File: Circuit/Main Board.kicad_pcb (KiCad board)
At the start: 2 copper layers, 120 x 120 mm, 200 parts, among them J1 Conn_Coaxial, J2 Conn_Coaxial, J3 Conn_Coaxial, J4 Conn_Coaxial, J5 Conn_01x02_Pin, J6 Conn_01x03_Pin, J7 Conn_01x02_Pin, J8 Conn_01x02_Pin, J9 Conn_01x05_Pin, K1 AGQ200A12, K2 AGQ200A12, K3 AGQ200A12, K4 AGQ200A12, K5 AGQ200A12, K6 AGQ200A12, K7 AGQ200A12, Q1 2N7002, Q2 TIP41C, Q3 TIP42C, Q4 TIP41C, Q5 TIP42C, Q6 TIP41C, Q7 TIP42C, U1 STM32G491CCUx, U10 OPA2197xD, U11 INA828D, U12 DG201, U13 OPA2197xD, U14 DG201, U15 OPA2376xxD, U16 INA828D, U17 DG201, U18 OPA2376xxD, U2 DG201, U3 OPA2197xD, U4 OPA2197xD, U5 OPA2197xD, U6 OPA2197xD, U7 ULN2003, U8 DG201, U9 OPA2376xxD, Y1 ECS-2520MV-xxx-xx

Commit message: Update Main Board.kicad_pcb
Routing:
- net /Auto-Balancing Bridge/In: track 141.8 -> 138.6 mm

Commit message: Update Main Board.kicad_pcb
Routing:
- net GND: vias 124 -> 130
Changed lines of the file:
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@@
 	)
 	(via
+		(at 158.877 89.027)
+		(size 0.6)
+		(drill 0.3)
+		(layers "F.Cu" "B.Cu")
+		(free yes)
+		(net 50)
+	)
+	(via
+		(at 150.368 151.13)
+		(size 0.6)
+		(drill 0.3)
+		(layers "F.Cu" "B.Cu")
+		(free yes)
+		(net 50)
+	)
+	(via
 		(at 88.392 140.97)
 		(size 0.6)
@@
 	)
 	(via
+		(at 158.877 125.73)
+		(size 0.6)
+		(drill 0.3)
+		(layers "F.Cu" "B.Cu")
+		(free yes)
+		(net 50)
+	)
+	(via
 		(at 88.265 44.45)
 		(size 0.6)
@@
 	)
 	(via
+		(at 147.32 154.94)
+		(size 0.6)
+		(drill 0.3)
+		(layers "F.Cu" "B.Cu")
+		(free yes)
+		(net 50)
+	)
+	(via
 		(at 115.57 86.36)
 		(size 0.6)
@@
 	)
 	(via
+		(at 153.162 144.78)
+		(size 0.6)
+		(drill 0.3)
+		(layers "F.Cu" "B.Cu")
+		(free yes)
+		(net 50)
+	)
+	(via
 		(at 113.157 64.262)
 		(size 0.6)
@@
 	)
 	(via
+		(at 153.67 154.94)
+		(size 0.6)
+		(drill 0.3)
+		(layers "F.Cu" "B.Cu")
+		(free yes)
+		(net 50)
+	)
+	(via
 		(at 99.695 62.865)
 		(size 0.6)
@@
 	)
 	(segment
-		(start 149.479 149.479)
-		(end 149.479 153.659886)
+		(start 144.78 147.701)
+		(end 147.955 147.701)
 		(width 0.5)
 		(layer "F.Cu")
@@
 	)
 	(segment
-		(start 140.8195 143.7405)
-		(end 144.399 147.32)
+		(start 148.717 157.226)
+		(end 149.479 156.464)
 		(width 0.5)
 		(layer "F.Cu")
@@
 	)
 	(segment
-		(start 148.717 157.226)
-		(end 149.479 156.464)
+		(start 149.479 156.464)
+		(end 149.479 153.659886)
 		(width 0.5)
 		(layer "F.Cu")
@@
 	)
 	(segment
-		(start 149.479 156.464)
-		(end 149.479 153.659886)
+		(start 140.8195 130.175)
+		(end 140.8195 143.7405)
 		(width 0.5)
 		(layer "F.Cu")
@@
 	)
 	(segment
-		(start 144.399 147.32)
-		(end 147.32 147.32)
+		(start 149.479 149.225)
+		(end 149.479 153.659886)
 		(width 0.5)
 		(layer "F.Cu")
@@
 	)
 	(segment
-		(start 140.8195 130.175)
-		(end 140.8195 143.7405)
+		(start 140.8195 143.7405)
+		(end 144.78 147.701)
 		(width 0.5)
 		(layer "F.Cu")
@@
 	)
 	(segment
-		(start 147.32 147.32)
-		(end 149.479 149.479)
+		(start 147.955 147.701)
+		(end 149.479 149.225)
 		(width 0.5)
 		(layer "F.Cu")
@@
 		(min_thickness 0.25)
 		(filled_areas_thickness no)
-		(fill
+		(fill yes
 			(thermal_gap 0.5)
 			(thermal_bridge_width 0.5)
@@
 		(min_thickness 0.25)
 		(filled_areas_thickness no)
-		(fill
+		(fill yes
 			(thermal_gap 0.5)
 			(thermal_bridge_width 0.5)

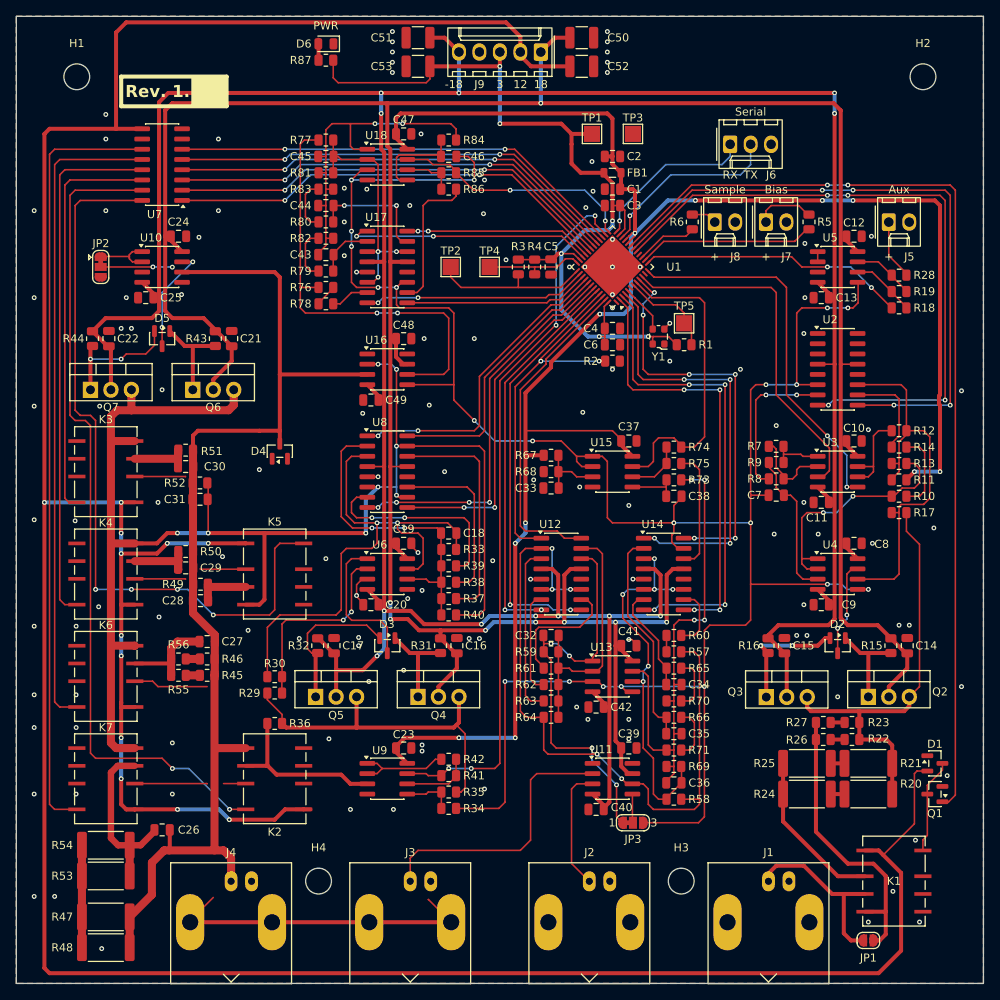
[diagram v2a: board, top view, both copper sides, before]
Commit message: Input Protection Second Attempt
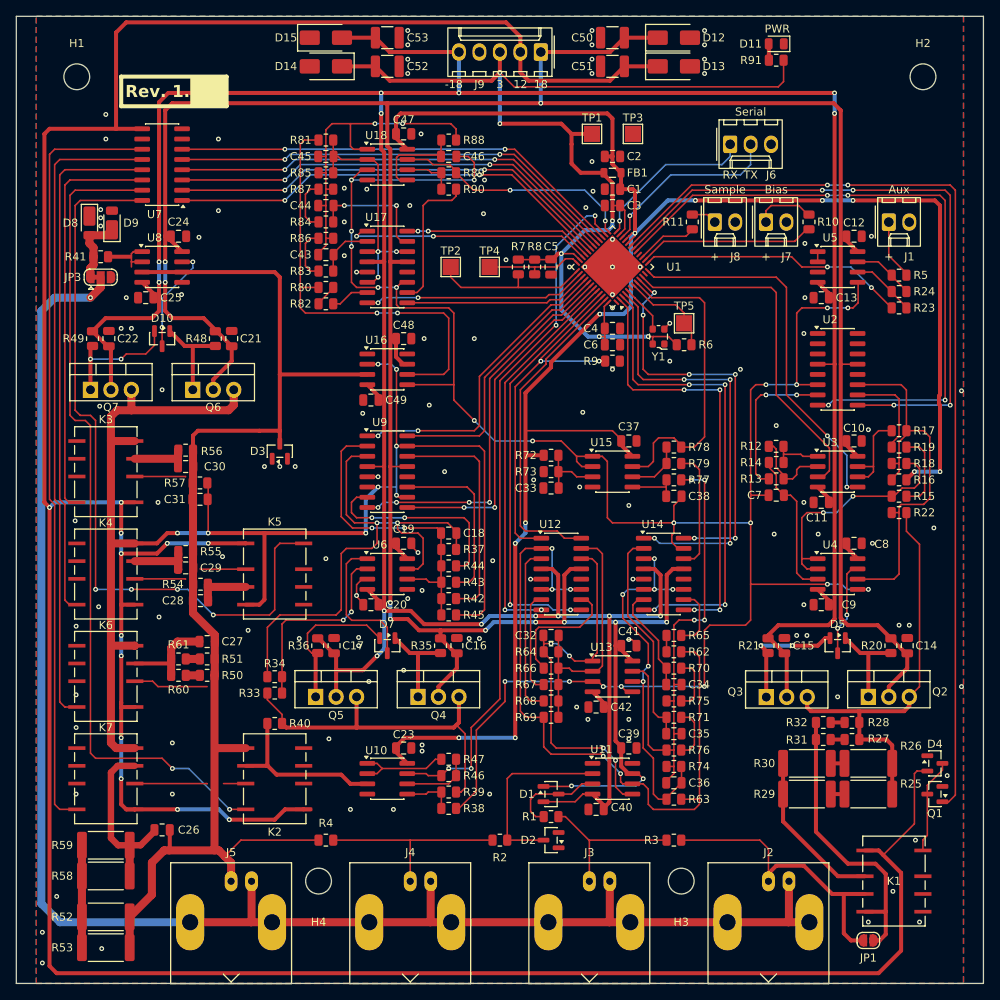
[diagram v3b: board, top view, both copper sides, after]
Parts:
- removed the C51 at (91.4, 45.2)
- removed the D4 at (74.3, 96.5)
- removed JP2: SolderJumper_3_Bridged12, Jumper:SolderJumper-3_P1.3mm_Bridged12_RoundedPad1.0x1.5mm
- removed the R28 at (151.1, 74.7)
- added C53: 22u, Capacitor_SMD:C_1210_3225Metric, F.Cu at (87.6, 45.2)
- added D1: BAV199, Package_TO_SOT_SMD:SOT-23, F.Cu at (108.0, 139.1)
- added D12: TBD, Diode_SMD:D_SMA, F.Cu at (123.2, 45.2)
- added D13: TBD, Diode_SMD:D_SMA, F.Cu at (123.2, 48.8)
- added D14: TBD, Diode_SMD:D_SMA, F.Cu at (80.0, 48.8)
- added D15: TBD, Diode_SMD:D_SMA, F.Cu at (80.0, 45.2)
- added D2: BAV199, Package_TO_SOT_SMD:SOT-23, F.Cu at (108.0, 144.8)
- added D3: BAV199, Package_TO_SOT_SMD:SOT-23, F.Cu at (74.3, 96.5)
- added D8: DFLS240LX, Diode_SMD:D_PowerDI-123, F.Cu at (50.7, 68.2)
- added D9: DFLS240LX, Diode_SMD:D_PowerDI-123, F.Cu at (53.5, 68.2)
- added R1: 1k, Resistor_SMD:R_0805_2012Metric, F.Cu at (108.0, 141.9)
- added R2: 1k, Resistor_SMD:R_0805_2012Metric, F.Cu at (101.6, 144.8)
- added R3: 100k, Resistor_SMD:R_0805_2012Metric, F.Cu at (123.2, 144.8)
- added R4: 100k, Resistor_SMD:R_0805_2012Metric, F.Cu at (80.0, 144.8)
- added R41: 50, Resistor_SMD:R_0805_2012Metric, F.Cu at (52.1, 72.4)
- added R5: 50, Resistor_SMD:R_0805_2012Metric, F.Cu at (151.1, 74.7)
- JP3: footprint Jumper:SolderJumper-3_P1.3mm_Bridged12_RoundedPad1.0x1.5mm_NumberLabels -> Jumper:SolderJumper-3_P1.3mm_Bridged12_RoundedPad1.0x1.5mm
- moved JP3 94.6 mm to (52.1, 74.9)
- moved D11 55.9 mm to (135.9, 46.0)
- moved R91 55.9 mm to (135.9, 48.0)
- moved C52 3.81 mm to (87.6, 48.8), turned to 180 degrees
- moved C50 3.81 mm to (115.6, 45.2), turned to 0 degrees
- moved C51 3.81 mm to (115.6, 48.8), turned to 0 degrees
- renumbered C52 to C51, C53 to C52, D5 to D10, D6 to D11, D1 to D4, D2 to D5, D3 to D7, J5 to J1, J1 to J2, J2 to J3, J3 to J4, J4 to J5, R5 to R10, R6 to R11, R7 to R12, R8 to R13, R9 to R14, R10 to R15, R11 to R16, R12 to R17, R13 to R18, R14 to R19, R15 to R20, R16 to R21, R17 to R22, R18 to R23, R19 to R24, R20 to R25, R21 to R26, R22 to R27, R23 to R28, R24 to R29, R25 to R30, R26 to R31, R27 to R32, R29 to R33, R30 to R34, R31 to R35, R32 to R36, R33 to R37, R34 to R38, R35 to R39, R36 to R40, R37 to R42, R38 to R43, R39 to R44, R40 to R45, R41 to R46, R42 to R47, R43 to R48, R44 to R49, R45 to R50, R46 to R51, R47 to R52, R48 to R53, R49 to R54, R50 to R55, R51 to R56, R52 to R57, R53 to R58, R54 to R59, R1 to R6, R55 to R60, R56 to R61, R57 to R62, R58 to R63, R59 to R64, R60 to R65, R61 to R66, R62 to R67, R63 to R68, R64 to R69, R3 to R7, R65 to R70, R66 to R71, R67 to R72, R68 to R73, R69 to R74, R70 to R75, R71 to R76, R73 to R77, R74 to R78, R75 to R79, R4 to R8, R76 to R80, R77 to R81, R78 to R82, R79 to R83, R80 to R84, R81 to R85, R82 to R86, R83 to R87, R84 to R88, R85 to R89, R2 to R9, R86 to R90, R87 to R91, U9 to U10, U10 to U8, U8 to U9
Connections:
- C26 pad 1: /Auto-Balancing Bridge/In -> /Auto-Balancing Bridge/TIA_SUM
- C27 pad 1: /Auto-Balancing Bridge/In -> /Auto-Balancing Bridge/TIA_SUM
- C28 pad 1: /Auto-Balancing Bridge/In -> /Auto-Balancing Bridge/TIA_SUM
- C29 pad 1: /Auto-Balancing Bridge/In -> /Auto-Balancing Bridge/TIA_SUM
- C30 pad 1: /Auto-Balancing Bridge/In -> /Auto-Balancing Bridge/TIA_SUM
- C31 pad 1: /Auto-Balancing Bridge/In -> /Auto-Balancing Bridge/TIA_SUM
- C32 pad 1: Net-(JP3-A) -> Net-(U11-Ref)
- J1 pad 1: /Signal Source/Aux_Out -> Net-(J1-Pin_1)
- J2 pad 2: GND -> GUARD EXT
- J3 pad 1: /Voltage Amplifier/In+ -> Net-(J3-In)
- J3 pad 2: GND -> GUARD EXT
- J4 pad 1: /Voltage Amplifier/In- -> Net-(J4-In)
- J4 pad 2: GUARD -> GUARD EXT
- J5 pad 1: /Auto-Balancing Bridge/In -> /Auto-Balancing Bridge/TIA_SUM
- J5 pad 2: GUARD -> GUARD EXT
- JP3 pad 1: Net-(JP3-A) -> Net-(D8-A)
- JP3 pad 2: Net-(JP3-C) -> GUARD EXT
- JP3 pad 3: +1.65VA -> GND
- K2 pad 5: /Auto-Balancing Bridge/In -> /Auto-Balancing Bridge/TIA_SUM
- K3 pad 2: GUARD -> unconnected-(K3-Pad2)
- K4 pad 2: GUARD -> unconnected-(K4-Pad2)
- K5 pad 2: GUARD -> unconnected-(K5-Pad2)
- K6 pad 2: GUARD -> unconnected-(K6-Pad2)
- K7 pad 2: GUARD -> unconnected-(K7-Pad2)
- R24 pad 2: Net-(R19-Pad2) (its old number) -> /Signal Source/Aux_Out
- R50 pad 1: /Auto-Balancing Bridge/In -> /Auto-Balancing Bridge/TIA_SUM
- R51 pad 1: /Auto-Balancing Bridge/In -> /Auto-Balancing Bridge/TIA_SUM
- R52 pad 1: /Auto-Balancing Bridge/In -> /Auto-Balancing Bridge/TIA_SUM
- R53 pad 1: /Auto-Balancing Bridge/In -> /Auto-Balancing Bridge/TIA_SUM
- R54 pad 1: /Auto-Balancing Bridge/In -> /Auto-Balancing Bridge/TIA_SUM
- R55 pad 1: /Auto-Balancing Bridge/In -> /Auto-Balancing Bridge/TIA_SUM
- R56 pad 1: /Auto-Balancing Bridge/In -> /Auto-Balancing Bridge/TIA_SUM
- R57 pad 1: /Auto-Balancing Bridge/In -> /Auto-Balancing Bridge/TIA_SUM
- R64 pad 1: Net-(JP3-A) -> Net-(U11-Ref)
- U11 pad 5: Net-(JP3-C) -> Net-(U11-Ref)
- U12 pad 14: Net-(JP3-A) -> Net-(U11-Ref)
- U13 pad 1: Net-(JP3-A) -> Net-(U11-Ref)
- U16 pad 3: /Auto-Balancing Bridge/In -> /Auto-Balancing Bridge/TIA_SUM
- U5 pad 7: Net-(R19-Pad2) (its old number) -> /Signal Source/Aux_Out
- U8 pad 1: Net-(JP2-A) -> GUARD
- U8 pad 2: Net-(JP2-A) -> GUARD
- U8 pad 3: GND -> /Auto-Balancing Bridge/TIA_SUM
- U8 pad 6: /Auto-Balancing Bridge/In -> /Auto-Balancing Bridge/TIA_SUM
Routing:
- net GUARD EXT: track 0.00 -> 200.7 mm, vias 0 -> 1
- net /Auto-Balancing Bridge/TIA_SUM: track 0.00 -> 155.7 mm
- net /Auto-Balancing Bridge/In: track 138.6 -> 0.00 mm
- net Net-(JP3-A): track 51.3 -> 0.00 mm, vias 4 -> 0
- net Net-(U11-Ref): track 0.00 -> 49.8 mm, vias 0 -> 4
- net +3.3V: track 112.4 -> 147.2 mm
- net +1.65VA: track 287.4 -> 260.5 mm
- net +18V: track 388.6 -> 413.9 mm, vias 8 -> 12
- net Net-(J4-In): track 0.00 -> 24.9 mm
- net Net-(J3-In): track 0.00 -> 19.8 mm
- net -18V: track 406.2 -> 423.6 mm, vias 12 -> 14
- net /Signal Source/Out: track 22.4 -> 37.7 mm
- net +12V: track 417.6 -> 430.3 mm
- net /Voltage Amplifier/In-: track 34.2 -> 23.1 mm
- net GUARD: track 505.5 -> 515.3 mm, vias 2 -> 0
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
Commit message: New Resistor Selection Circuit
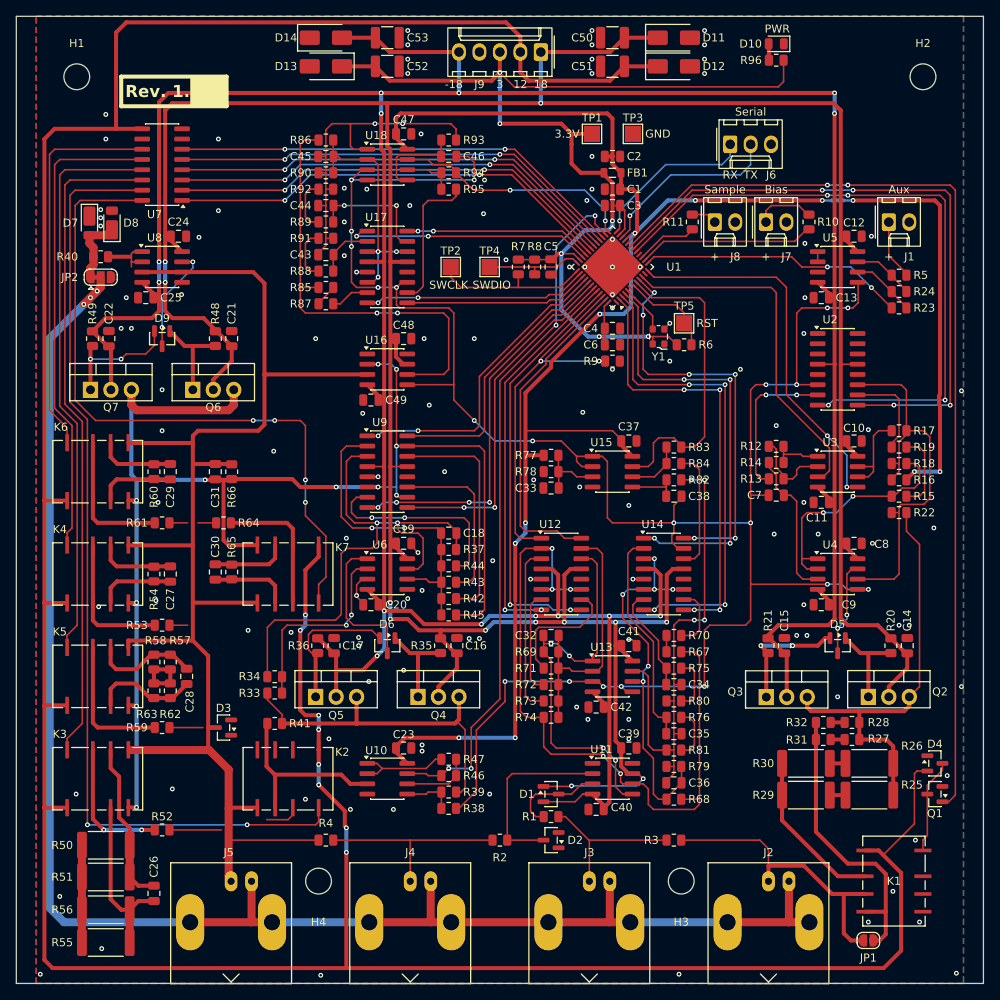
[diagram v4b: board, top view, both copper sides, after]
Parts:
- added R52: 100k, Resistor_SMD:R_0805_2012Metric, F.Cu at (59.7, 143.5)
- added R53: 100k, Resistor_SMD:R_0805_2012Metric, F.Cu at (59.7, 118.1)
- added R59: 100k, Resistor_SMD:R_0805_2012Metric, F.Cu at (59.7, 130.8)
- added R61: 100k, Resistor_SMD:R_0805_2012Metric, F.Cu at (59.7, 105.4)
- added R64: 100k, Resistor_SMD:R_0805_2012Metric, F.Cu at (67.3, 105.4)
- moved D3 35.0 mm to (67.3, 130.8), turned to 180 degrees
- moved R50 8.89 mm to (52.7, 145.4)
- moved R51 8.76 mm to (52.7, 149.4)
- moved R55 8.25 mm to (52.7, 157.5)
- moved R56 8.00 mm to (52.7, 153.4)
- moved C26 7.94 mm to (58.7, 151.4), turned to -90 degrees
- moved R58 6.61 mm to (58.7, 122.7), turned to -90 degrees
- moved C28 5.01 mm to (62.7, 124.5), turned to -90 degrees
- moved R63 4.98 mm to (58.7, 126.2), turned to -90 degrees
- moved R57 4.86 mm to (60.7, 122.7), turned to -90 degrees
- moved R54 4.83 mm to (58.7, 111.8), turned to -90 degrees
- moved R60 4.76 mm to (58.7, 99.1), turned to -90 degrees
- moved R66 4.18 mm to (68.3, 99.1), turned to -90 degrees
- moved R65 4.16 mm to (68.3, 111.5), turned to 90 degrees
- moved C30 4.00 mm to (66.3, 111.5), turned to 90 degrees
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- renumbered C29 to C27, C27 to C28, C30 to C29, C28 to C30, D11 to D10, D12 to D11, D13 to D12, D14 to D13, D15 to D14, D7 to D6, D8 to D7, D9 to D8, D10 to D9, JP3 to JP2, K7 to K3, K6 to K5, K3 to K6, K5 to K7, R41 to R40, R40 to R41, R52 to R50, R53 to R51, R55 to R54, R58 to R55, R59 to R56, R50 to R57, R51 to R58, R56 to R60, R60 to R62, R61 to R63, R54 to R65, R57 to R66, R62 to R67, R63 to R68, R64 to R69, R65 to R70, R66 to R71, R67 to R72, R68 to R73, R69 to R74, R70 to R75, R71 to R76, R72 to R77, R73 to R78, R74 to R79, R75 to R80, R76 to R81, R77 to R82, R78 to R83, R79 to R84, R80 to R85, R81 to R86, R82 to R87, R83 to R88, R84 to R89, R85 to R90, R86 to R91, R87 to R92, R88 to R93, R89 to R94, R90 to R95, R91 to R96
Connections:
- C26 pad 1: /Auto-Balancing Bridge/TIA_SUM -> Net-(C26-Pad1)
- C27 pad 1: /Auto-Balancing Bridge/TIA_SUM -> Net-(C27-Pad1)
- C28 pad 1: /Auto-Balancing Bridge/TIA_SUM -> Net-(C28-Pad1)
- C29 pad 1: /Auto-Balancing Bridge/TIA_SUM -> Net-(C29-Pad1)
- C30 pad 1: /Auto-Balancing Bridge/TIA_SUM -> Net-(C30-Pad1)
- K3 pad 2: unconnected-(K7-Pad2) -> Net-(K3-Pad2)
- K3 pad 5: unconnected-(K7-Pad5) -> /Auto-Balancing Bridge/TIA_SUM
- K3 pad 6: unconnected-(K7-Pad6) -> Net-(C26-Pad1)
- K3 pad 7: unconnected-(K7-Pad7) -> Net-(K3-Pad2)
- K4 pad 2: unconnected-(K4-Pad2) -> Net-(K4-Pad2)
- K4 pad 5: unconnected-(K4-Pad5) -> /Auto-Balancing Bridge/TIA_SUM
- K4 pad 6: unconnected-(K4-Pad6) -> Net-(C27-Pad1)
- K4 pad 7: unconnected-(K4-Pad7) -> Net-(K4-Pad2)
- K5 pad 2: unconnected-(K6-Pad2) -> Net-(K5-Pad2)
- K5 pad 5: unconnected-(K6-Pad5) -> /Auto-Balancing Bridge/TIA_SUM
- K5 pad 6: unconnected-(K6-Pad6) -> Net-(C28-Pad1)
- K5 pad 7: unconnected-(K6-Pad7) -> Net-(K5-Pad2)
- K6 pad 2: unconnected-(K3-Pad2) -> Net-(K6-Pad2)
- K6 pad 5: unconnected-(K3-Pad5) -> /Auto-Balancing Bridge/TIA_SUM
- K6 pad 6: unconnected-(K3-Pad6) -> Net-(C29-Pad1)
- K6 pad 7: unconnected-(K3-Pad7) -> Net-(K6-Pad2)
- K7 pad 2: unconnected-(K5-Pad2) -> Net-(K7-Pad2)
- K7 pad 5: unconnected-(K5-Pad5) -> /Auto-Balancing Bridge/TIA_SUM
- K7 pad 6: unconnected-(K5-Pad6) -> Net-(C30-Pad1)
- K7 pad 7: unconnected-(K5-Pad7) -> Net-(K7-Pad2)
- R50 pad 1: /Auto-Balancing Bridge/TIA_SUM -> Net-(C26-Pad1)
- R51 pad 1: /Auto-Balancing Bridge/TIA_SUM -> Net-(C26-Pad1)
- R54 pad 1: /Auto-Balancing Bridge/TIA_SUM -> Net-(C27-Pad1)
- R57 pad 1: /Auto-Balancing Bridge/TIA_SUM -> Net-(C28-Pad1)
- R57 pad 2: Net-(R50-Pad2) (its old number) -> Net-(R57-Pad2)
- R58 pad 1: /Auto-Balancing Bridge/TIA_SUM -> Net-(C28-Pad1)
- R58 pad 2: Net-(R51-Pad2) -> Net-(R57-Pad2)
- R60 pad 1: /Auto-Balancing Bridge/TIA_SUM -> Net-(C29-Pad1)
- R62 pad 1: Net-(R50-Pad2) (its old number) -> Net-(R57-Pad2)
- R63 pad 1: Net-(R51-Pad2) -> Net-(R57-Pad2)
- R65 pad 1: /Auto-Balancing Bridge/TIA_SUM -> Net-(C30-Pad1)
- U1 pad 27: /Auto-Balancing Bridge/R_SEL_10 -> /Auto-Balancing Bridge/R_SEL_100k
- U1 pad 28: /Auto-Balancing Bridge/R_SEL_100 -> /Auto-Balancing Bridge/R_SEL_10k
- U1 pad 29: /Auto-Balancing Bridge/DC_INT_ISO -> /Auto-Balancing Bridge/R_SEL_100
- U1 pad 30: /Auto-Balancing Bridge/R_SEL_100k -> /Auto-Balancing Bridge/R_SEL_10
- U1 pad 31: /Auto-Balancing Bridge/R_SEL_1k -> /Auto-Balancing Bridge/DC_INT_ISO
- U1 pad 32: /Auto-Balancing Bridge/R_SEL_10k -> /Auto-Balancing Bridge/R_SEL_1k
- U7 pad 1: /Auto-Balancing Bridge/R_SEL_10k -> /Auto-Balancing Bridge/R_SEL_1k
- U7 pad 11: /Auto-Balancing Bridge/SEL_10 -> /Auto-Balancing Bridge/SEL_100k
- U7 pad 12: /Auto-Balancing Bridge/SEL_100 -> /Auto-Balancing Bridge/SEL_10k
- U7 pad 13: /Auto-Balancing Bridge/SEL_10k -> /Auto-Balancing Bridge/SEL_100
- U7 pad 14: /Auto-Balancing Bridge/SEL_100k -> /Auto-Balancing Bridge/SEL_10
- U7 pad 2: /Auto-Balancing Bridge/R_SEL_1k -> /Auto-Balancing Bridge/DC_INT_ISO
- U7 pad 3: /Auto-Balancing Bridge/R_SEL_100k -> /Auto-Balancing Bridge/R_SEL_10
- U7 pad 4: /Auto-Balancing Bridge/DC_INT_ISO -> /Auto-Balancing Bridge/R_SEL_100
- U7 pad 5: /Auto-Balancing Bridge/R_SEL_100 -> /Auto-Balancing Bridge/R_SEL_10k
- U7 pad 6: /Auto-Balancing Bridge/R_SEL_10 -> /Auto-Balancing Bridge/R_SEL_100k
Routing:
- net GUARD: track 515.3 -> 550.9 mm
- net +12V: track 430.3 -> 405.0 mm, vias 12 -> 8
- net /Auto-Balancing Bridge/TIA_SUM: track 155.7 -> 176.0 mm
- net Net-(C26-Pad1): track 0.00 -> 20.1 mm
- net Net-(K4-Pad2): track 0.00 -> 17.3 mm
- net Net-(K5-Pad2): track 0.00 -> 17.3 mm
- net Net-(K6-Pad2): track 0.00 -> 17.3 mm
- net Net-(K7-Pad2): track 0.00 -> 17.2 mm
- net Net-(K3-Pad2): track 0.00 -> 16.8 mm, vias 0 -> 2
- net /Auto-Balancing Bridge/DC_ISO: track 102.4 -> 118.8 mm
- net /Auto-Balancing Bridge/SEL_10: track 95.7 -> 81.6 mm
- net Net-(C28-Pad1): track 0.00 -> 13.2 mm
- net /Auto-Balancing Bridge/OUT+: track 184.8 -> 174.8 mm, vias 8 -> 11
- net /Auto-Balancing Bridge/SEL_100: track 80.4 -> 70.6 mm
- net Net-(C30-Pad1): track 0.00 -> 9.87 mm
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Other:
- board text added: "3.3V"
- board text added: "GND"
- board text added: "RST"
